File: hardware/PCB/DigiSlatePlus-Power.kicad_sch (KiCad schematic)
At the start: 29 parts, among them Q2 FS8205A, U11 KA78M05_TO252, U12 LM2596S-ADJ, U13 LD1117S33TR_SOT223, U14 TP4056, U15 DW01A

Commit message: change page structure
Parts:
- renumbered C12 to C10, C13 to C11, C16 to C12, C4 to C13, C6 to C14, C8 to C15, C9 to C16, C10 to C17, C11 to C18, C14 to C19, C15 to C20, C5 to C8, C7 to C9, D7 to D10, D8 to D9, Q2 to Q3, R10 to R17, R8 to R18, R9 to R19, R7 to R20, R12 to R21, R11 to R22, RV2 to RV4, U12 to U21, U15 to U22, U14 to U23, U11 to U24, U13 to U25

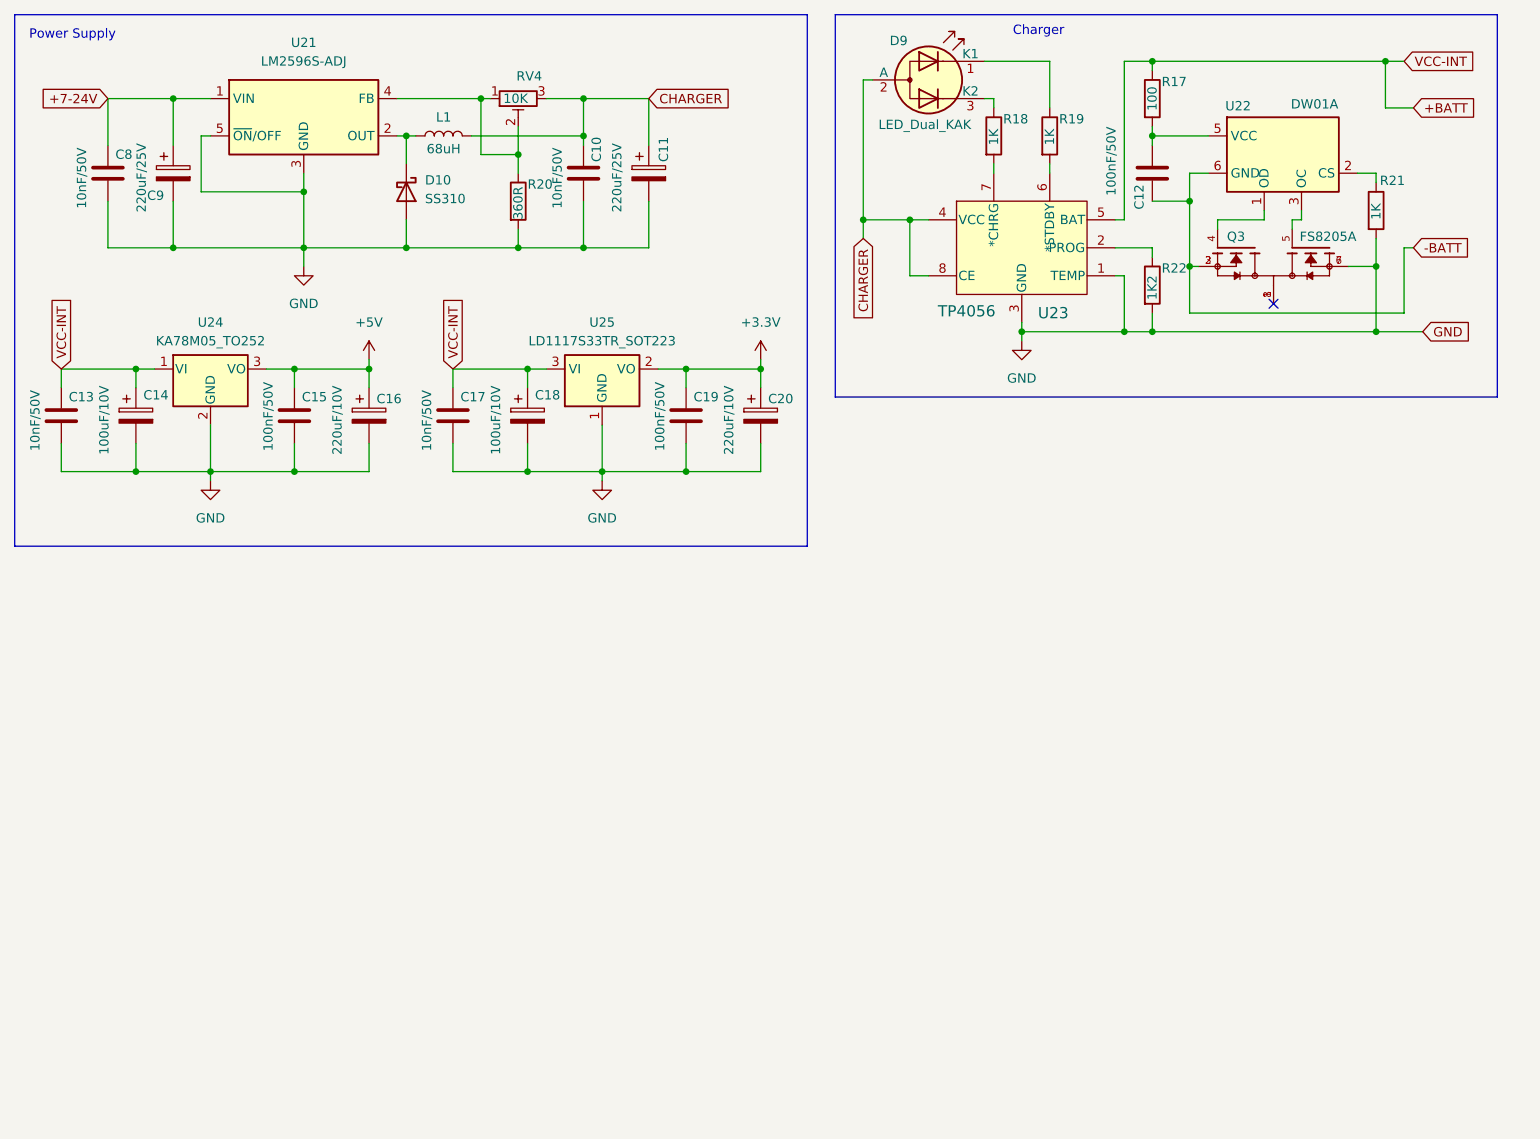
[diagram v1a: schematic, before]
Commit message: schematic and board layout finished
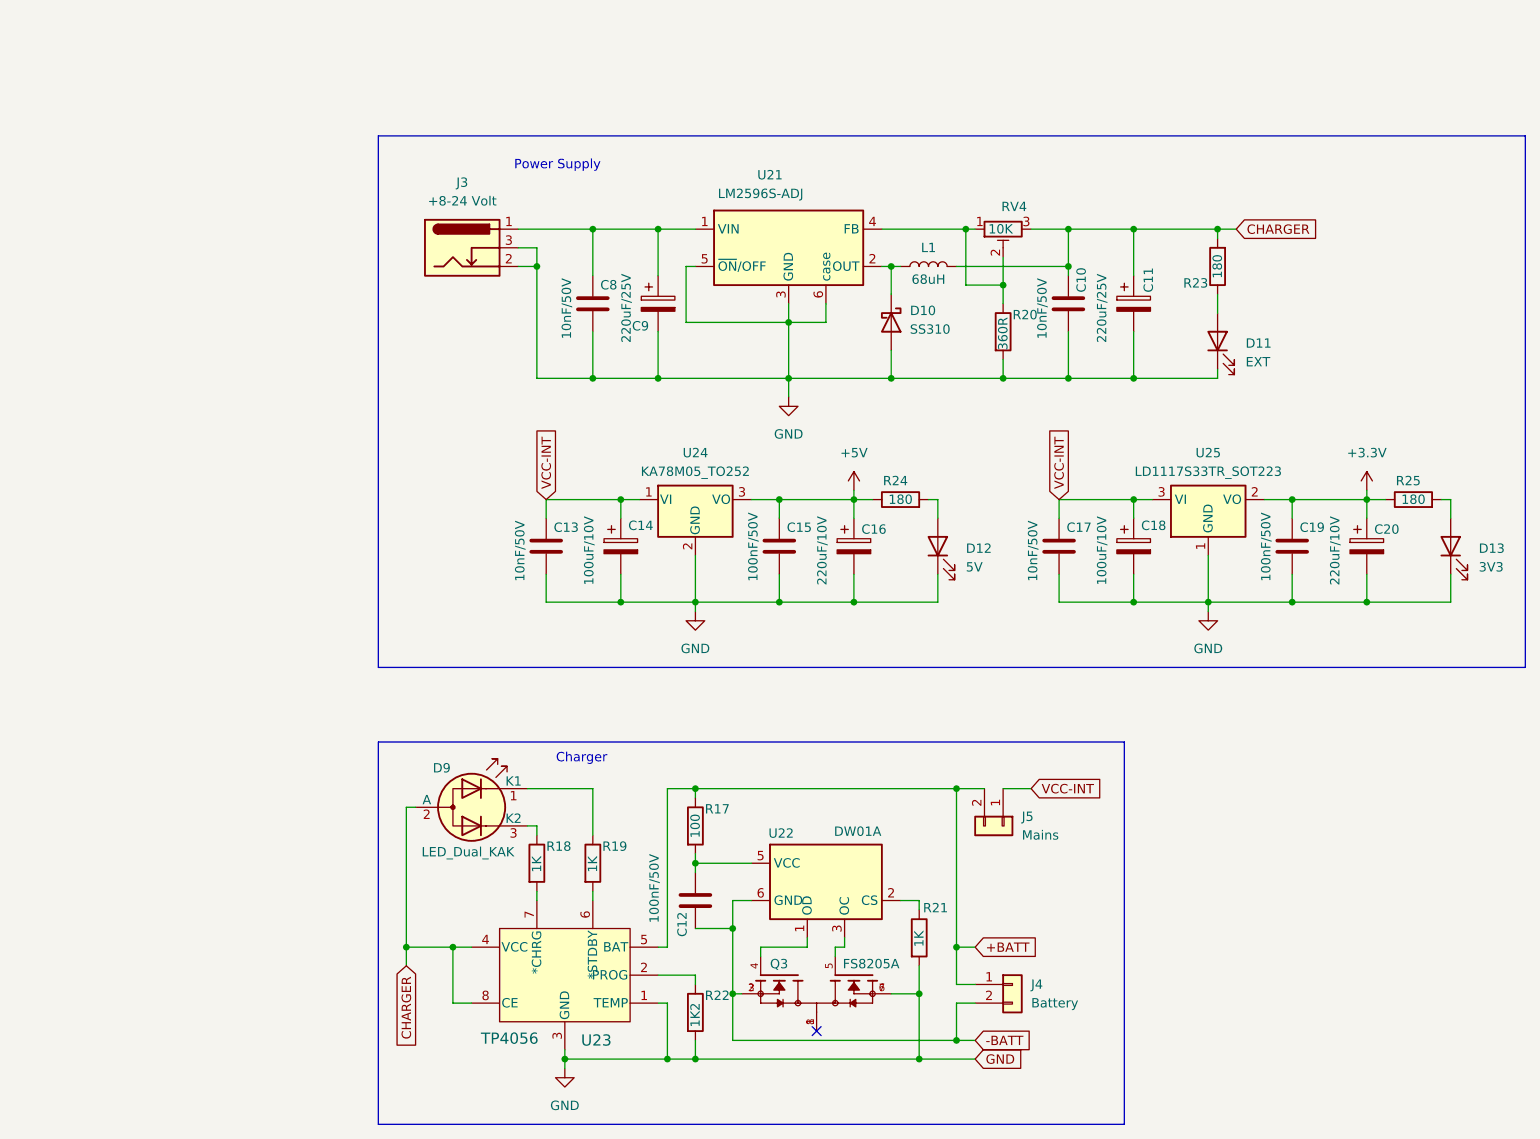
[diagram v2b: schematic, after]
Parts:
- added D11: EXT, LED_SMD:LED_0201_0603Metric_Pad0.64x0.40mm_HandSolder, symbol Device:LED
- added D12: 5V, LED_SMD:LED_0201_0603Metric_Pad0.64x0.40mm_HandSolder, symbol Device:LED
- added D13: 3V3, LED_SMD:LED_0201_0603Metric_Pad0.64x0.40mm_HandSolder, symbol Device:LED
- added J3: +8-24 Volt, Connector_BarrelJack:BarrelJack_GCT_DCJ200-10-A_Horizontal, symbol Connector:Barrel_Jack_Switch
- added J4: Battery, Connector_JST:JST_XH_B2B-XH-AM_1x02_P2.50mm_Vertical, symbol Connector_Generic:Conn_01x02
- added J5: Mains, Connector_JST:JST_XH_B2B-XH-AM_1x02_P2.50mm_Vertical, symbol Connector_Generic:Conn_01x02
- added R23, R24, R25: 180, Resistor_SMD:R_0805_2012Metric_Pad1.20x1.40mm_HandSolder, symbol Device:R
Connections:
- net +3.3V: now also R25.1
- net +5V: now also R24.1
- net +BATT: now also J4.1 (Pin_1), J5.2 (Pin_2); no longer C13.1, C14.1, C17.1, C18.1, U24.1 (VI), U25.3 (VI)
- net -BATT: now also J4.2 (Pin_2)
- net CHARGER: now also R23.2
- net GND: now also U21.6 (case), D11.1 (K), D12.1 (K), D13.1 (K), J3.2, J3.3
- net +7-24V: no longer names the net of C8.1, C9.1, U21.1 (VIN)
- net +7-24V: now also J3.1
- new net: D12.2 (A), R24.2
- new net: D11.2 (A), R23.1
- new net: D13.2 (A), R25.2
- new net VCC-INT: C13.1, C14.1, C17.1, C18.1, J5.1 (Pin_1), U24.1 (VI), U25.3 (VI)
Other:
- moved on the sheet: C10, C11, C12, C13, C14, C15, C16, C17, C18, C19, C20, C8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
